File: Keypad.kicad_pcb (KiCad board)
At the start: 2 copper layers, 109 x 57.2 mm, 46 parts, among them J1 10118193-0001LF, J2 M20-9750446, Q1 BC32725TA, SW1 MX1A-11NN, SW2 MX1A-11NN, SW3 MX1A-11NN, SW4 MX1A-11NN, SW5 MX1A-11NN, SW6 MX1A-11NN, SW7 MX1A-11NN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

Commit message: Updates
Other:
- board text added: "KEYPAD_V01"
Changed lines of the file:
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@@
   (general
     (thickness 1.6)
-    (drawings 10)
+    (drawings 11)
     (tracks 246)
     (zones 0)
@@
   (layers
     (0 F.Cu signal)
-    (31 B.Cu signal hide)
+    (31 B.Cu signal)
     (32 B.Adhes user)
     (33 F.Adhes user)
@@
     (36 B.SilkS user)
     (37 F.SilkS user)
-    (38 B.Mask user)
+    (38 B.Mask user hide)
     (39 F.Mask user)
     (40 Dwgs.User user)
     (41 Cmts.User user)
-    (42 Eco1.User user)
-    (43 Eco2.User user)
+    (42 Eco1.User user hide)
+    (43 Eco2.User user hide)
     (44 Edge.Cuts user)
     (45 Margin user hide)
@@
     )
   )
+  (gr_text "KEYPAD_V01 " (at 148.844 58.039) (layer Dwgs.User)
+    (effects (font (size 5 5) (thickness 0.45)))
+  )
   (gr_text +3V3 (at 97.3074 84.328) (layer F.SilkS)
     (effects (font (size 1.5 1.5) (thickness 0.2)))
@@
   )
   (dimension 57.15 (width 0.15) (layer Dwgs.User)
-    (gr_text "57.15 mm" (at 222.90088 94.97314 270) (layer Dwgs.User)
+    (gr_text "57.15 mm" (at 210.814 94.97314 270) (layer Dwgs.User)
       (effects (font (size 3 3) (thickness 0.4)))
     )
-    (feature1 (pts (xy 198.2089 123.54814) (xy 220.987301 123.54814)))
-    (feature2 (pts (xy 198.2089 66.39814) (xy 220.987301 66.39814)))
-    (crossbar (pts (xy 220.40088 66.39814) (xy 220.40088 123.54814)))
-    (arrow1a (pts (xy 220.40088 123.54814) (xy 219.814459 122.421636)))
-    (arrow1b (pts (xy 220.40088 123.54814) (xy 220.987301 122.421636)))
-    (arrow2a (pts (xy 220.40088 66.39814) (xy 219.814459 67.524644)))
-    (arrow2b (pts (xy 220.40088 66.39814) (xy 220.987301 67.524644)))
+    (feature1 (pts (xy 198.2089 123.54814) (xy 207.850421 123.54814)))
+    (feature2 (pts (xy 198.2089 66.39814) (xy 207.850421 66.39814)))
+    (crossbar (pts (xy 207.264 66.39814) (xy 207.264 123.54814)))
+    (arrow1a (pts (xy 207.264 123.54814) (xy 206.677579 122.421636)))
+    (arrow1b (pts (xy 207.264 123.54814) (xy 207.850421 122.421636)))
+    (arrow2a (pts (xy 207.264 66.39814) (xy 206.677579 67.524644)))
+    (arrow2b (pts (xy 207.264 66.39814) (xy 207.850421 67.524644)))
   )
   (dimension 108.966 (width 0.15) (layer Dwgs.User)
-    (gr_text 109mm (at 143.7259 147.75996) (layer Dwgs.User)
+    (gr_text 109mm (at 143.7259 135.553) (layer Dwgs.User)
       (effects (font (size 3 3) (thickness 0.45)))
     )
-    (feature1 (pts (xy 198.2089 123.54814) (xy 198.2089 145.046381)))
-    (feature2 (pts (xy 89.2429 123.54814) (xy 89.2429 145.046381)))
-    (crossbar (pts (xy 89.2429 144.45996) (xy 198.2089 144.45996)))
-    (arrow1a (pts (xy 198.2089 144.45996) (xy 197.082396 145.046381)))
-    (arrow1b (pts (xy 198.2089 144.45996) (xy 197.082396 143.873539)))
-    (arrow2a (pts (xy 89.2429 144.45996) (xy 90.369404 145.046381)))
-    (arrow2b (pts (xy 89.2429 144.45996) (xy 90.369404 143.873539)))
+    (feature1 (pts (xy 198.2089 123.54814) (xy 198.2089 132.539421)))
+    (feature2 (pts (xy 89.2429 123.54814) (xy 89.2429 132.539421)))
+    (crossbar (pts (xy 89.2429 131.953) (xy 198.2089 131.953)))
+    (arrow1a (pts (xy 198.2089 131.953) (xy 197.082396 132.539421)))
+    (arrow1b (pts (xy 198.2089 131.953) (xy 197.082396 131.366579)))
+    (arrow2a (pts (xy 89.2429 131.953) (xy 90.369404 132.539421)))
+    (arrow2b (pts (xy 89.2429 131.953) (xy 90.369404 131.366579)))
   )
   (gr_line (start 198.2089 66.39814) (end 198.2089 123.54814) (layer Edge.Cuts) (width 0.05))

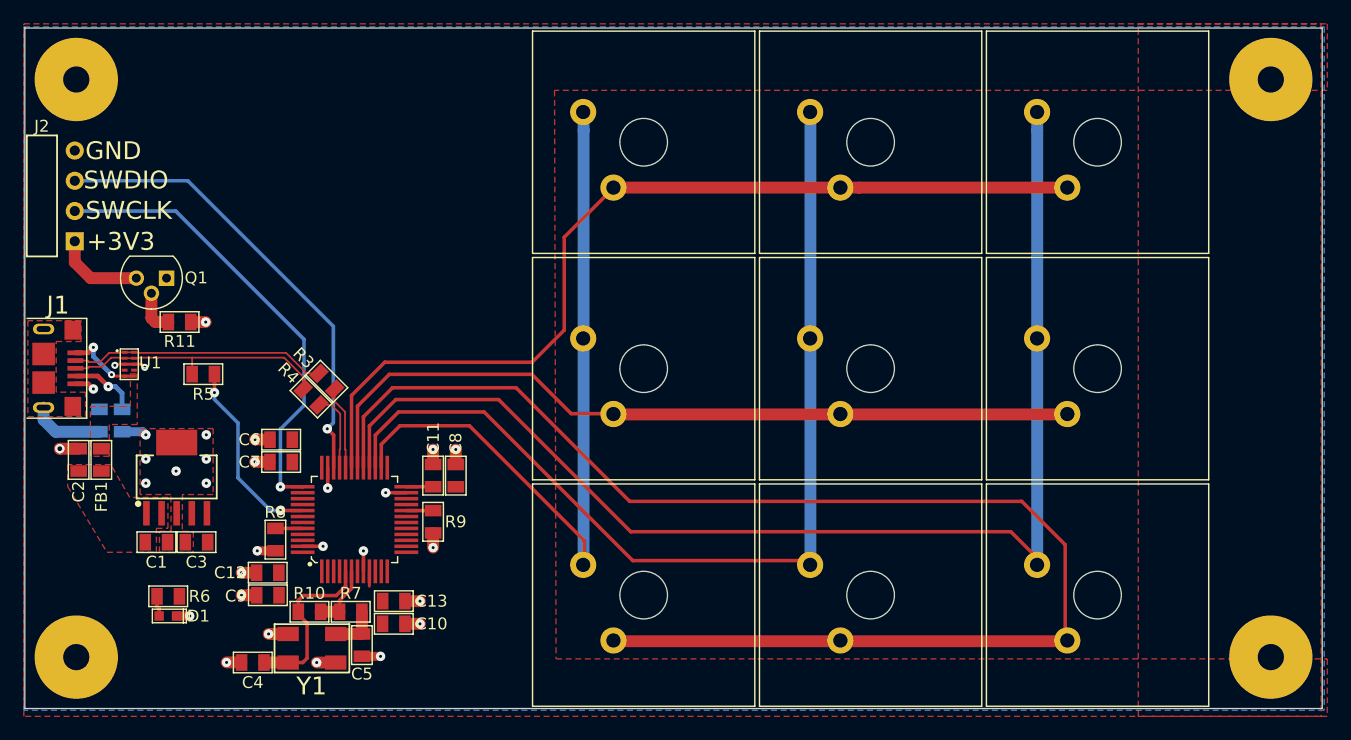
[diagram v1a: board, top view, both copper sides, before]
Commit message: Minor measurement fixes
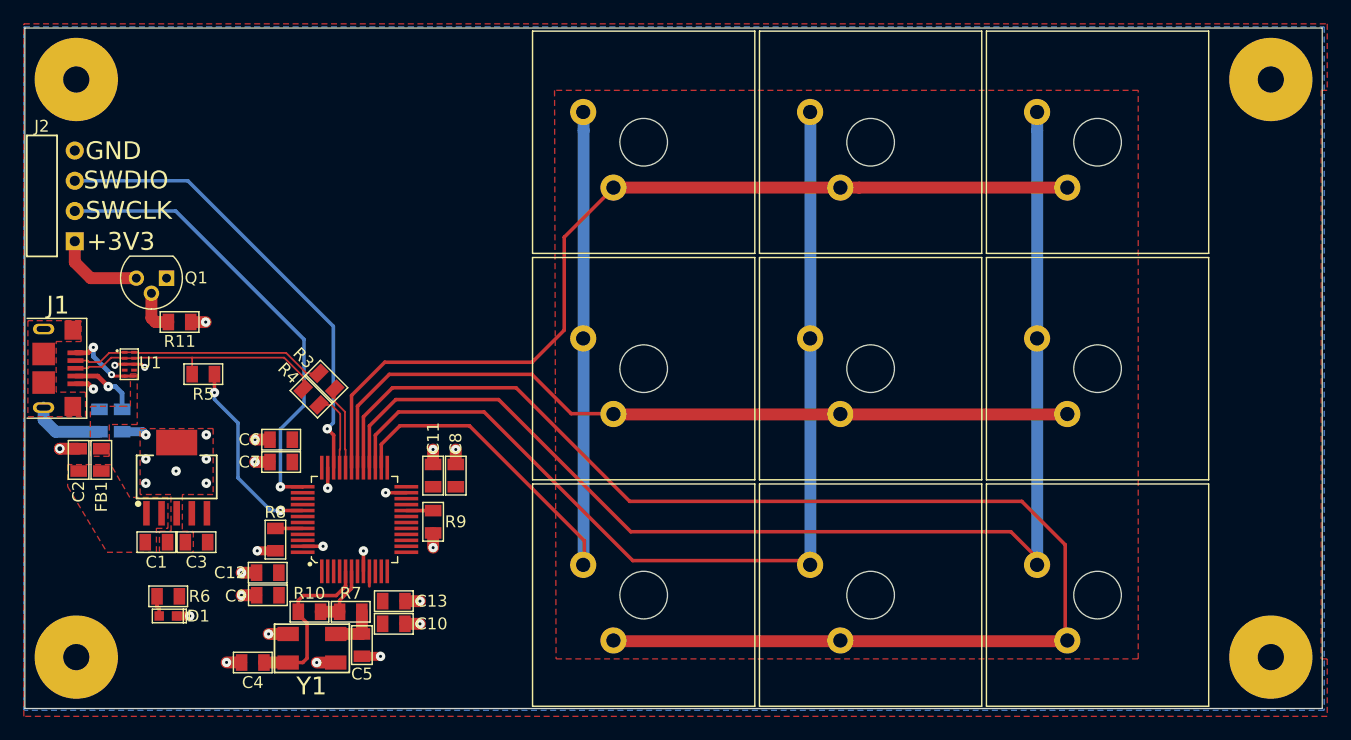
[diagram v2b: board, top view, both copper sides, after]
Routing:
- net VDDA: track 3.51 -> 1.26 mm
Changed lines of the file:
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@@
   (general
     (thickness 1.6)
-    (drawings 11)
-    (tracks 246)
+    (drawings 13)
+    (tracks 245)
     (zones 0)
     (modules 46)
@@
     (mod_text_size 1 1)
     (mod_text_width 0.15)
-    (pad_size 0.975 1.4)
+    (pad_size 0.3 2)
     (pad_drill 0)
     (pad_to_mask_clearance 0.051)
@@
     (fp_line (start 1 -0.6) (end 1 0.6) (layer F.Fab) (width 0.1))
     (pad 1 smd rect (at -0.9375 0 180) (size 0.975 1.4) (layers F.Cu F.Paste F.Mask)
-      (net 48 VDDA) (solder_mask_margin 0.075))
+      (net 48 VDDA) (solder_mask_margin 0.075) (zone_connect 2))
     (pad 2 smd rect (at 0.9375 0 180) (size 0.975 1.4) (layers F.Cu F.Paste F.Mask)
       (net 2 GND) (solder_mask_margin 0.075))
@@
     )
   )
+  (dimension 100.368103 (width 0.15) (layer Dwgs.User)
+    (gr_text "100.35 mm" (at 143.742571 131.68635 360) (layer Dwgs.User)
+      (effects (font (size 3 3) (thickness 0.4)))
+    )
+    (feature1 (pts (xy 193.929 119.253) (xy 193.926784 128.9842)))
+    (feature2 (pts (xy 93.5609 119.23014) (xy 93.558684 128.96134)))
+    (crossbar (pts (xy 93.558817 128.37492) (xy 193.926917 128.39778)))
+    (arrow1a (pts (xy 193.926917 128.39778) (xy 192.80028 128.983944)))
+    (arrow1b (pts (xy 193.926917 128.39778) (xy 192.800547 127.811103)))
+    (arrow2a (pts (xy 93.558817 128.37492) (xy 94.685187 128.961597)))
+    (arrow2b (pts (xy 93.558817 128.37492) (xy 94.685454 127.788756)))
+  )
+  (dimension 48.514 (width 0.15) (layer Dwgs.User)
+    (gr_text "48.5 mm" (at 205.484 94.996 270) (layer Dwgs.User)
+      (effects (font (size 3 3) (thickness 0.4)))
+    )
+    (feature1 (pts (xy 193.929 119.253) (xy 202.770421 119.253)))
+    (feature2 (pts (xy 193.929 70.739) (xy 202.770421 70.739)))
+    (crossbar (pts (xy 202.184 70.739) (xy 202.184 119.253)))
+    (arrow1a (pts (xy 202.184 119.253) (xy 201.597579 118.126496)))
+    (arrow1b (pts (xy 202.184 119.253) (xy 202.770421 118.126496)))
+    (arrow2a (pts (xy 202.184 70.739) (xy 201.597579 71.865504)))
+    (arrow2b (pts (xy 202.184 70.739) (xy 202.770421 71.865504)))
+  )
   (gr_text "KEYPAD_V01 " (at 148.844 58.039) (layer Dwgs.User)
     (effects (font (size 5 5) (thickness 0.45)))
@@
   )
   (dimension 57.15 (width 0.15) (layer Dwgs.User)
-    (gr_text "57.15 mm" (at 210.814 94.97314 270) (layer Dwgs.User)
+    (gr_text "57.15 mm" (at 212.084 94.97314 270) (layer Dwgs.User)
       (effects (font (size 3 3) (thickness 0.4)))
     )
-    (feature1 (pts (xy 198.2089 123.54814) (xy 207.850421 123.54814)))
-    (feature2 (pts (xy 198.2089 66.39814) (xy 207.850421 66.39814)))
-    (crossbar (pts (xy 207.264 66.39814) (xy 207.264 123.54814)))
-    (arrow1a (pts (xy 207.264 123.54814) (xy 206.677579 122.421636)))
-    (arrow1b (pts (xy 207.264 123.54814) (xy 207.850421 122.421636)))
-    (arrow2a (pts (xy 207.264 66.39814) (xy 206.677579 67.524644)))
-    (arrow2b (pts (xy 207.264 66.39814) (xy 207.850421 67.524644)))
+    (feature1 (pts (xy 198.2089 123.54814) (xy 209.120421 123.54814)))
+    (feature2 (pts (xy 198.2089 66.39814) (xy 209.120421 66.39814)))
+    (crossbar (pts (xy 208.534 66.39814) (xy 208.534 123.54814)))
+    (arrow1a (pts (xy 208.534 123.54814) (xy 207.947579 122.421636)))
+    (arrow1b (pts (xy 208.534 123.54814) (xy 209.120421 122.421636)))
+    (arrow2a (pts (xy 208.534 66.39814) (xy 207.947579 67.524644)))
+    (arrow2b (pts (xy 208.534 66.39814) (xy 209.120421 67.524644)))
   )
   (dimension 108.966 (width 0.15) (layer Dwgs.User)
-    (gr_text 109mm (at 143.7259 135.553) (layer Dwgs.User)
+    (gr_text "109 mm" (at 143.7259 139.617) (layer Dwgs.User)
       (effects (font (size 3 3) (thickness 0.45)))
     )
-    (feature1 (pts (xy 198.2089 123.54814) (xy 198.2089 132.539421)))
-    (feature2 (pts (xy 89.2429 123.54814) (xy 89.2429 132.539421)))
-    (crossbar (pts (xy 89.2429 131.953) (xy 198.2089 131.953)))
-    (arrow1a (pts (xy 198.2089 131.953) (xy 197.082396 132.539421)))
-    (arrow1b (pts (xy 198.2089 131.953) (xy 197.082396 131.366579)))
-    (arrow2a (pts (xy 89.2429 131.953) (xy 90.369404 132.539421)))
-    (arrow2b (pts (xy 89.2429 131.953) (xy 90.369404 131.366579)))
+    (feature1 (pts (xy 198.2089 123.54814) (xy 198.2089 136.603421)))
+    (feature2 (pts (xy 89.2429 123.54814) (xy 89.2429 136.603421)))
+    (crossbar (pts (xy 89.2429 136.017) (xy 198.2089 136.017)))
+    (arrow1a (pts (xy 198.2089 136.017) (xy 197.082396 136.603421)))
+    (arrow1b (pts (xy 198.2089 136.017) (xy 197.082396 135.430579)))
+    (arrow2a (pts (xy 89.2429 136.017) (xy 90.369404 136.603421)))
+    (arrow2b (pts (xy 89.2429 136.017) (xy 90.369404 135.430579)))
   )
   (gr_line (start 198.2089 66.39814) (end 198.2089 123.54814) (layer Edge.Cuts) (width 0.05))
@@
   (segment (start 119.29086 114.53368) (end 119.2934 114.53114) (width 0.25) (layer F.Cu) (net 48))
   (segment (start 121.28248 104.92256) (end 121.2819 104.92314) (width 0.25) (layer F.Cu) (net 48))
-  (segment (start 123.53036 104.92256) (end 121.28248 104.92256) (width 0.3) (layer F.Cu) (net 48))
   (segment (start 118.1789 112.02614) (end 118.1789 113.27614) (width 0.25) (layer F.Cu) (net 48))
   (via (at 96.24822 96.5073) (size 0.8) (drill 0.25) (layers F.Cu B.Cu) (net 49))
@@
     (polygon
       (pts
-        (xy 89.154 66.04) (xy 198.628 66.04) (xy 198.628 71.628) (xy 133.731 71.628) (xy 133.858 119.38)
-        (xy 198.628 119.38) (xy 198.628 124.206) (xy 89.154 124.206)
+        (xy 198.628 71.628) (xy 198.12 71.628) (xy 198.12 119.38) (xy 198.628 119.38) (xy 198.628 124.206)
+        (xy 89.154 124.206) (xy 89.154 66.04) (xy 198.628 66.04)
       )
     )
-  )
-  (zone (net 48) (net_name VDDA) (layer F.Cu) (hatch edge 0.508)
-    (connect_pads thru_hole_only (clearance 0.25))
-    (min_thickness 0.254)
-    (fill yes (arc_segments 32) (thermal_gap 0.508) (thermal_bridge_width 0.508))
     (polygon
       (pts
-        (xy 182.753 66.04) (xy 198.12 66.04) (xy 198.12 124.206) (xy 182.753 124.206)
+        (xy 133.731 71.628) (xy 133.858 119.38) (xy 182.753 119.38) (xy 182.753 71.628)
       )
     )
